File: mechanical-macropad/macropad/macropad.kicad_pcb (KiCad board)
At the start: 2 copper layers, 76 x 176.4 mm, 93 parts, among them J1 USB_B_Micro, J2 AVR-ISP-6, K1 KEYSW, K10 KEYSW, K11 KEYSW, K12 KEYSW, K13 KEYSW, K14 KEYSW, K15 KEYSW, K16 KEYSW, K17 KEYSW, K18 KEYSW, K19 KEYSW, K2 KEYSW, K20 KEYSW, K21 KEYSW, K22 KEYSW, K23 KEYSW, K24 KEYSW, K25 KEYSW, K26 KEYSW, K27 KEYSW, K28 KEYSW, K3 KEYSW, K4 KEYSW, K5 KEYSW, K6 KEYSW, K7 KEYSW, K8 KEYSW, K9 KEYSW, SW1 SW_Push, U1 ATMEGA32U4, X1 XTAL_GND

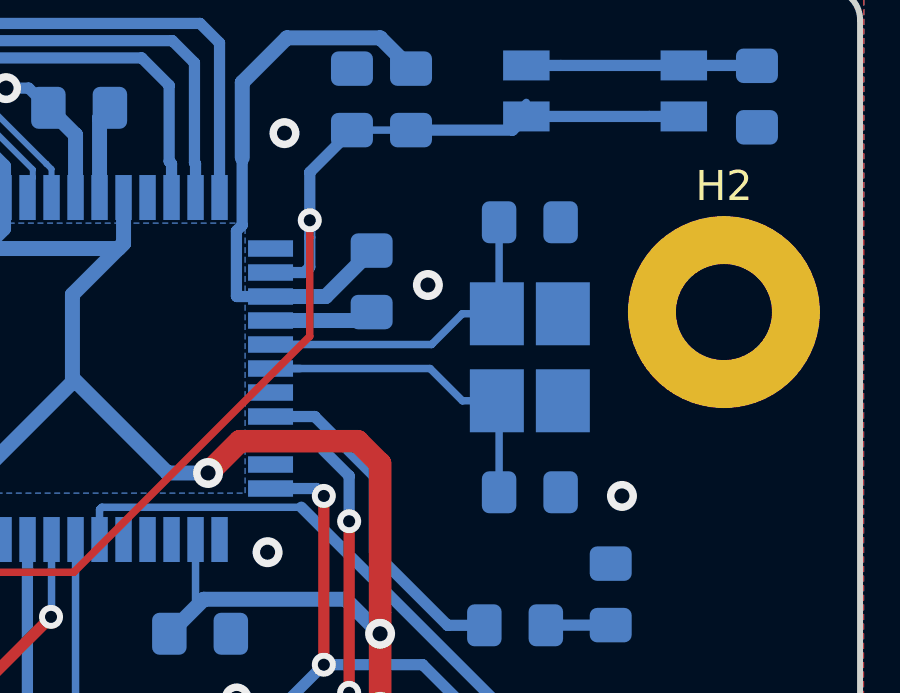
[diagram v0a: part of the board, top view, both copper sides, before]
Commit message: BUG: fix crystal footprint
Somehow it got messed up in the assembled revision. This commit fixes it
in a somewhat slapdash manner. Pull requests on this matter are welcome.
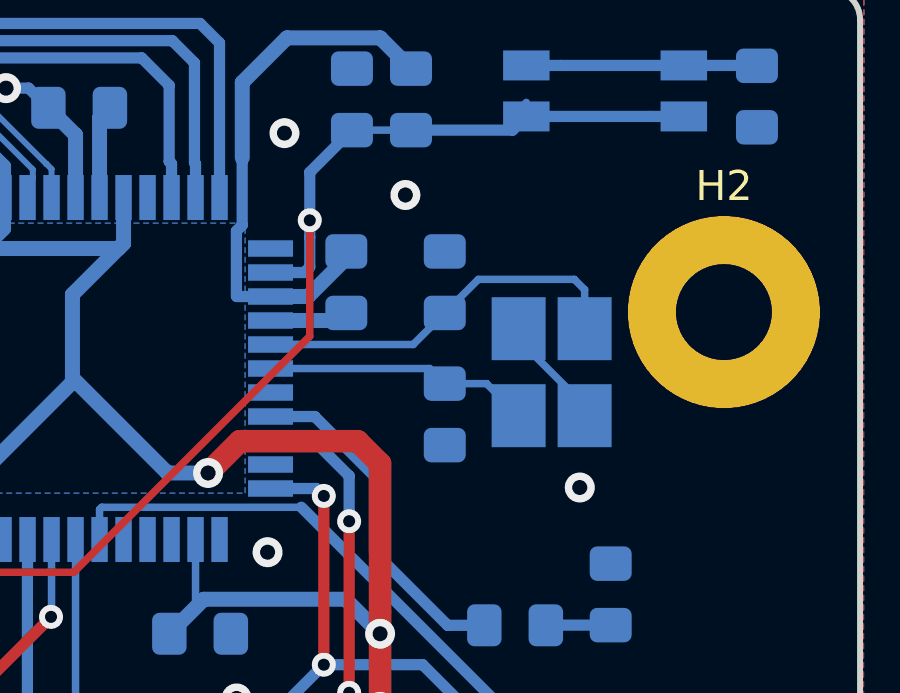
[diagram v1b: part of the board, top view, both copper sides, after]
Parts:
- removed X1: XTAL_GND, Crystal:Crystal_SMD_SeikoEpson_FA238-4Pin_3.2x2.5mm_HandSoldering
- added Y1: Crystal_GND24, Crystal:Crystal_SMD_SeikoEpson_FA238-4Pin_3.2x2.5mm_HandSoldering, B.Cu at (138.7, 39.5)
- R6: value 150R -> 330R
- moved C2 3.85 mm to (135.1, 40.9), turned to 270 degrees
- moved C1 3.47 mm to (135.1, 36.5), turned to 90 degrees
- moved C6 0.84 mm to (131.8, 36.5)
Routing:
- net Net-(C2-Pad1): track 12.1 -> 8.92 mm
- net GND: track 28.3 -> 31.3 mm
- net Net-(C1-Pad1): track 12.0 -> 13.8 mm
- net VCC: track 242.1 -> 241.3 mm

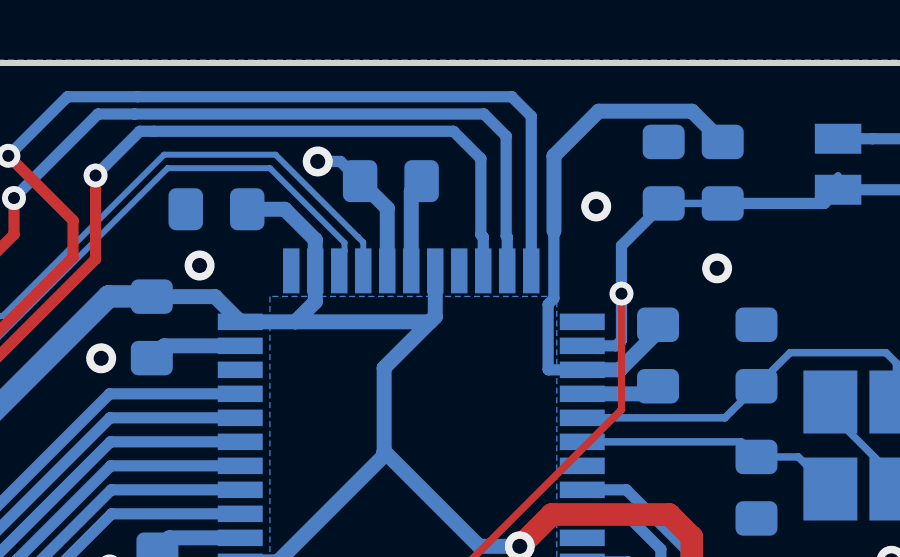
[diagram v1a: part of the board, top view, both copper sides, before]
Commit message: Tie slave select to ground
This is probably pointless, but it guarantees that SPI communication will work.
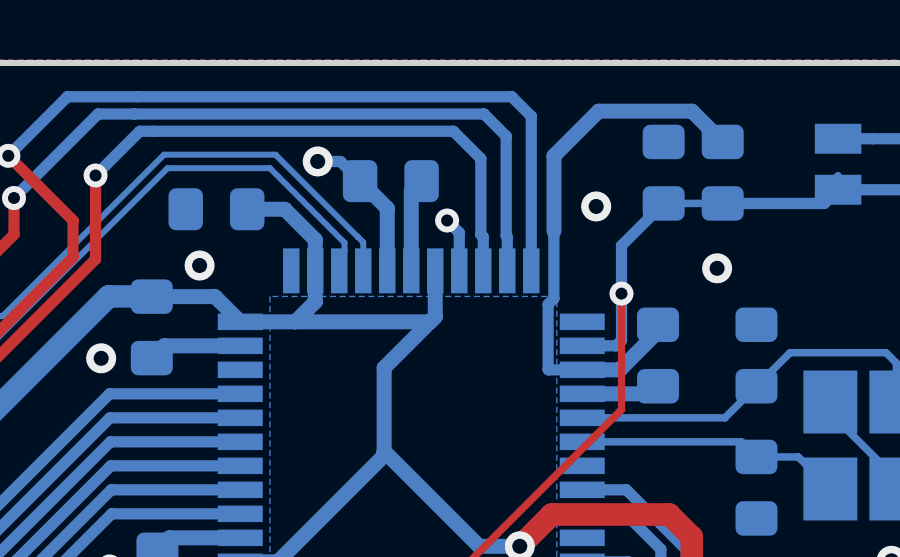
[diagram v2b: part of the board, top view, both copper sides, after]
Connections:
- U1 pad 8: Net-(U1-Pad8) -> GND
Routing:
- net GND: track 31.3 -> 33.2 mm, vias 49 -> 50

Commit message: bump version
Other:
- board text added: "Macropad v0.2 https://lfcode.ca"
- board text removed: "Macropad v0.1 https://lfcode.ca"
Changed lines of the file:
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@@
   (title_block
     (title "Custom Numpad/Macropad")
-    (date 2018-11-28)
-    (rev 0)
+    (date 2019-03-07)
+    (rev 0.2)
     (company lfcode.ca)
-    (comment 1 "Copyright (c) 2018 lf")
+    (comment 1 "Copyright (c) 2019 lf")
     (comment 2 "Licensed under TAPR Open Hardware License")
   )
@@
   )
   (setup
-    (last_trace_width 0.375)
+    (last_trace_width 0.25)
     (user_trace_width 0.375)
     (user_trace_width 0.5)
@@
       (net 55 Row7))
   )
-  (gr_text "Macropad v0.1\nhttps://lfcode.ca" (at 77.34375 30.84375) (layer F.SilkS)
+  (gr_text "Macropad v0.2\nhttps://lfcode.ca" (at 77.34375 30.84375) (layer F.SilkS)
     (effects (font (size 1 1) (thickness 0.15)) (justify left))
   )
